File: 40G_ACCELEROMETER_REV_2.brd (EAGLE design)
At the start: 18.8 x 24.1 mm, 30 parts, among them IC1 3.3V_LDO, IC2 X_BUFFER, IC3 Y_BUFFER, IC4 Z_BUFFER

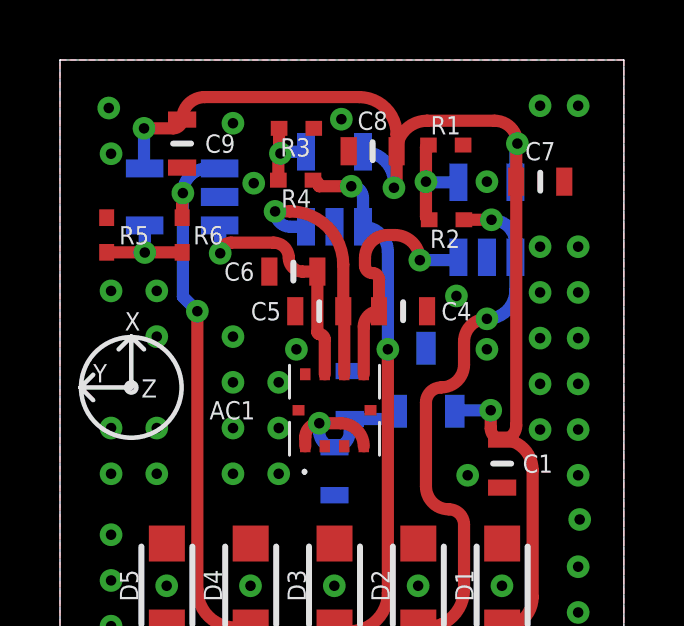
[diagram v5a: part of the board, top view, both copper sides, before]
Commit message: Changes to component label placement. Addition of more ground vias where room was found. Change in routing for power to X buffer
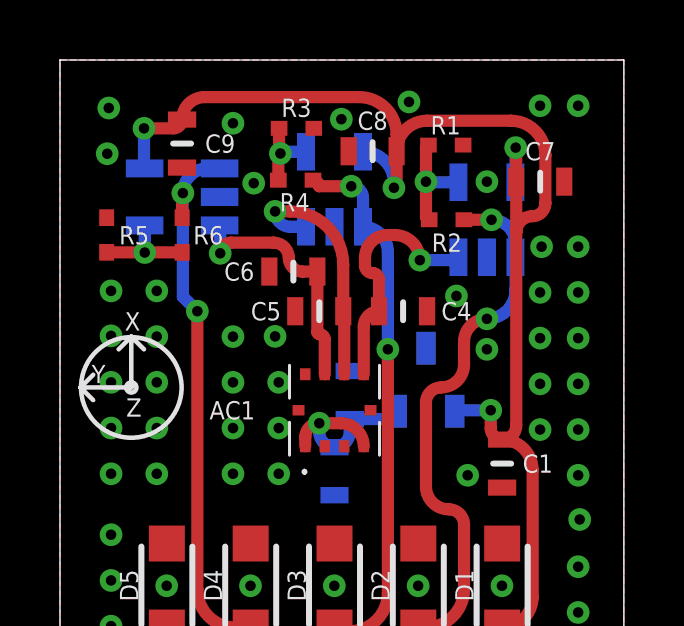
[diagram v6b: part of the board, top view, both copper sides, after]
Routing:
- net 12V: track 42.8 -> 46.4 mm
- net GND: vias 52 -> 56
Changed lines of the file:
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@@
 <wire x1="2.37683125" y1="14.908125" x2="2.800121875" y2="14.484834375" width="0.1524" layer="21"/>
 <wire x1="2.800121875" y1="14.484834375" x2="2.800121875" y2="14.48483125" width="0.1524" layer="21"/>
-<text x="2.7154625" y="12.876328125" size="0.6096" layer="21" font="vector">Z</text>
+<text x="2.2074625" y="12.241328125" size="0.6096" layer="21" font="vector">Z</text>
 <text x="2.159" y="15.113" size="0.6096" layer="21" font="vector">X</text>
-<text x="1.10695625" y="13.384275" size="0.6096" layer="21" font="vector">Y</text>
+<text x="1.05615625" y="13.358875" size="0.6096" layer="21" font="vector">Y</text>
 <text x="14.228975" y="22.019409375" size="0.6096" layer="22" font="vector" rot="MR180" align="center">X-AXIS</text>
 <text x="9.1494875" y="16.685946875" size="0.6096" layer="22" font="vector" rot="MR0" align="center">Y-AXIS</text>
@@
 <attribute name="MANUFACTURER_PART_NUMBER" value="TNPW04023K48BEED" x="12.8842" y="18.804278125" size="1.778" layer="27" rot="R180" display="off"/>
 <attribute name="MFR_NAME" value="Vishay" x="12.8842" y="18.804278125" size="1.778" layer="27" rot="R180" display="off"/>
-<attribute name="NAME" x="12.33388125" y="17.864478125" size="0.6096" layer="25" ratio="6" rot="SR0"/>
+<attribute name="NAME" x="12.89268125" y="18.042278125" size="0.6096" layer="25" ratio="6" rot="SR0" align="center"/>
 </element>
 <element name="R3" library="SamacSys_Parts" package="RES_TNPW0402_VIS" value="TNPW04021K24BEED" x="7.8804" y="21.852278125" smashed="yes">
@@
 <attribute name="MANUFACTURER_PART_NUMBER" value="TNPW04021K24BEED" x="7.8804" y="21.852278125" size="1.778" layer="27" display="off"/>
 <attribute name="MFR_NAME" value="Vishay" x="7.8804" y="21.852278125" size="1.778" layer="27" display="off"/>
-<attribute name="NAME" x="7.347" y="20.912478125" size="0.6096" layer="25" ratio="6" rot="SR0"/>
+<attribute name="NAME" x="7.8804" y="22.538078125" size="0.6096" layer="25" ratio="6" rot="SR0" align="center"/>
 </element>
 <element name="R4" library="SamacSys_Parts" package="RES_TNPW0402_VIS" value="TNPW04023K48BEED" x="7.855" y="20.125078125" smashed="yes" rot="R180">
@@
 <attribute name="MANUFACTURER_PART_NUMBER" value="TNPW04023K48BEED" x="7.855" y="20.125078125" size="1.778" layer="27" rot="R180" display="off"/>
 <attribute name="MFR_NAME" value="Vishay" x="7.855" y="20.125078125" size="1.778" layer="27" rot="R180" display="off"/>
-<attribute name="NAME" x="7.3724" y="19.210678125" size="0.6096" layer="25" ratio="6" rot="SR0"/>
+<attribute name="NAME" x="7.3216" y="19.083678125" size="0.6096" layer="25" ratio="6" rot="SR0"/>
 </element>
 <element name="R5" library="SamacSys_Parts" package="RES_TNPW0402_VIS" value="TNPW04021K24BEED" x="1.5558" y="18.296278125" smashed="yes" rot="R90">
@@
 <via x="14.2304" y="20.074278125" extent="1-16" drill="0.35"/>
 <via x="17.272" y="1.397" extent="1-16" drill="0.35"/>
-<via x="7.8804" y="14.486278125" extent="1-16" drill="0.35"/>
+<via x="7.1692" y="14.918078125" extent="1-16" drill="0.35"/>
 <via x="14.2304" y="14.486278125" extent="1-16" drill="0.35"/>
 <via x="5.7658" y="22.0218" extent="1-16" drill="0.35"/>
 <via x="1.6256" y="22.5298" extent="1-16" drill="0.35"/>
-<via x="1.7018" y="21.0058" extent="1-16" drill="0.35"/>
+<via x="1.5748" y="21.0058" extent="1-16" drill="0.35"/>
 <via x="1.7018" y="16.4338" extent="1-16" drill="0.35"/>
 <via x="3.2258" y="16.4338" extent="1-16" drill="0.35"/>
@@
 <via x="16.002" y="4.191" extent="1-16" drill="0.35"/>
 <via x="16.002" y="11.811" extent="1-16" drill="0.35"/>
-<via x="16.002" y="17.907" extent="1-16" drill="0.35"/>
+<via x="16.0528" y="17.907" extent="1-16" drill="0.35"/>
 <via x="16.002" y="16.383" extent="1-16" drill="0.35"/>
 <via x="16.002" y="14.859" extent="1-16" drill="0.35"/>
@@
 <via x="6.35" y="6.604" extent="1-16" drill="0.35"/>
 <via x="3.556" y="6.604" extent="1-16" drill="0.35"/>
+<via x="3.2258" y="13.3858" extent="1-16" drill="0.35"/>
+<via x="11.6332" y="22.733" extent="1-16" drill="0.35"/>
+<via x="1.7018" y="14.9352" extent="1-16" drill="0.35"/>
+<via x="1.7018" y="13.3858" extent="1-16" drill="0.35"/>
 </signal>
 <signal name="X_SIG">
@@
 <wire x1="8.6424" y1="14.994278125" x2="8.5788" y2="15.057878125" width="0.4064" layer="1" curve="-90"/>
 <wire x1="8.5788" y1="15.057878125" x2="8.5788" y2="17.077078125" width="0.4064" layer="1"/>
-<wire x1="8.5788" y1="17.077078125" x2="8.5788" y2="17.280278125" width="0.4064" layer="1"/>
 <wire x1="8.5788" y1="17.077078125" x2="8.0836" y2="17.077078125" width="0.4064" layer="1"/>
 <wire x1="8.0836" y1="17.077078125" x2="7.6264" y2="17.534278125" width="0.4064" layer="1" curve="-90"/>
@@
 <wire x1="11.2204" y1="21.090278125" x2="11.2204" y2="19.959878125" width="0.4064" layer="1"/>
 <wire x1="11.2204" y1="19.959878125" x2="11.1316" y2="19.871078125" width="0.4064" layer="1" curve="-90"/>
-<wire x1="12.2364" y1="22.106278125" x2="11.2204" y2="21.090278125" width="0.4064" layer="1" curve="90"/>
-<via x="15.2464" y="21.344278125" extent="1-16" drill="0.35"/>
-<wire x1="15.2084" y1="20.074278125" x2="15.2084" y2="21.306278125" width="0.4064" layer="1"/>
-<wire x1="15.2084" y1="21.306278125" x2="15.2464" y2="21.344278125" width="0.4064" layer="1" curve="-90"/>
-<wire x1="15.1804" y1="20.054278125" x2="15.1804" y2="21.278278125" width="0.4064" layer="16"/>
-<wire x1="15.1804" y1="21.278278125" x2="15.2464" y2="21.344278125" width="0.4064" layer="16" curve="-90"/>
-<wire x1="15.2084" y1="20.074278125" x2="15.2084" y2="11.946278125" width="0.4064" layer="1"/>
-<wire x1="15.2084" y1="11.946278125" x2="14.7384" y2="11.476278125" width="0.4064" layer="1" curve="-90"/>
+<wire x1="14.7384" y1="11.476278125" x2="15.2084" y2="11.946278125" width="0.4064" layer="1" curve="90"/>
 <wire x1="14.7384" y1="2.294278125" x2="14.7384" y2="5.212278125" width="0.4064" layer="1"/>
 <wire x1="14.7384" y1="5.212278125" x2="15.7544" y2="6.228278125" width="0.4064" layer="1" curve="90"/>
 <wire x1="15.7544" y1="10.460278125" x2="14.7384" y2="11.476278125" width="0.4064" layer="1" curve="90"/>
 <wire x1="15.7544" y1="6.228278125" x2="15.7544" y2="10.460278125" width="0.4064" layer="1"/>
-<wire x1="15.2464" y1="21.344278125" x2="14.4844" y2="22.106278125" width="0.4064" layer="1" curve="90"/>
-<wire x1="14.4844" y1="22.106278125" x2="12.2364" y2="22.106278125" width="0.4064" layer="1"/>
-<wire x1="11.2204" y1="21.090278125" x2="11.2204" y2="21.242678125" width="0.4064" layer="1"/>
 <via x="2.8004" y="21.852278125" extent="1-16" drill="0.35"/>
 <wire x1="4.0704" y1="22.144278125" x2="3.7784" y2="21.852278125" width="0.4064" layer="1" curve="-90"/>
@@
 <wire x1="13.1584" y1="12.420278125" x2="13.1924" y2="12.454278125" width="0.4064" layer="16" curve="-90"/>
 <wire x1="13.1924" y1="12.454278125" x2="14.3574" y2="12.454278125" width="0.4064" layer="16"/>
-<wire x1="11.2204" y1="21.090278125" x2="11.2204" y2="21.649078125" width="0.4064" layer="1"/>
 <wire x1="11.2204" y1="21.649078125" x2="9.9758" y2="22.893678125" width="0.4064" layer="1" curve="90"/>
 <wire x1="4.8198" y1="22.893678125" x2="4.0704" y2="22.144278125" width="0.4064" layer="1" curve="90"/>
 <wire x1="9.9758" y1="22.893678125" x2="4.8198" y2="22.893678125" width="0.4064" layer="1"/>
+<wire x1="15.2084" y1="11.946278125" x2="15.2084" y2="18.3834" width="0.4064" layer="1"/>
+<wire x1="15.748" y1="18.923" x2="15.2084" y2="18.3834" width="0.4064" layer="1" curve="90"/>
+<wire x1="15.748" y1="18.923" x2="16.1798" y2="19.3548" width="0.4064" layer="1" curve="90"/>
+<wire x1="16.1798" y1="19.3548" x2="16.1798" y2="20.955" width="0.4064" layer="1"/>
+<wire x1="16.1798" y1="20.955" x2="15.028521875" y2="22.106278125" width="0.4064" layer="1" curve="90"/>
+<wire x1="15.028521875" y1="22.106278125" x2="12.2364" y2="22.106278125" width="0.4064" layer="1"/>
+<via x="15.1892" y="21.209" extent="1-16" drill="0.35"/>
+<wire x1="15.2084" y1="18.3834" x2="15.2084" y2="20.074278125" width="0.4064" layer="1"/>
+<wire x1="15.2084" y1="20.074278125" x2="15.2084" y2="21.1898" width="0.4064" layer="1"/>
+<wire x1="15.2084" y1="21.1898" x2="15.1892" y2="21.209" width="0.4064" layer="1" curve="90"/>
+<wire x1="15.1804" y1="20.054278125" x2="15.1804" y2="21.2002" width="0.4064" layer="16"/>
+<wire x1="15.1804" y1="21.2002" x2="15.1892" y2="21.209" width="0.4064" layer="16" curve="90"/>
+<wire x1="11.2204" y1="21.090278125" x2="11.2204" y2="21.649078125" width="0.4064" layer="1"/>
+<wire x1="11.2204" y1="21.090278125" x2="12.2364" y2="22.106278125" width="0.4064" layer="1" curve="-90"/>
 </signal>
 <signal name="X_OUT">

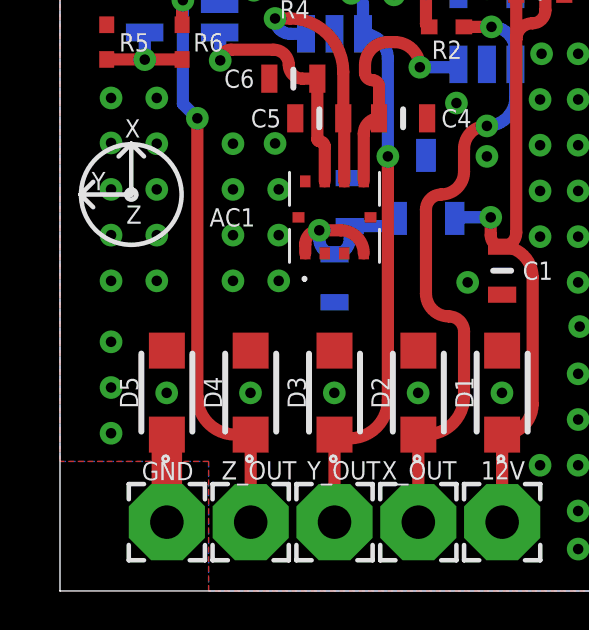
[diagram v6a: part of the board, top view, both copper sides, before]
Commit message: Widened GND path near diode. Enlarged Z dot for board orientation.
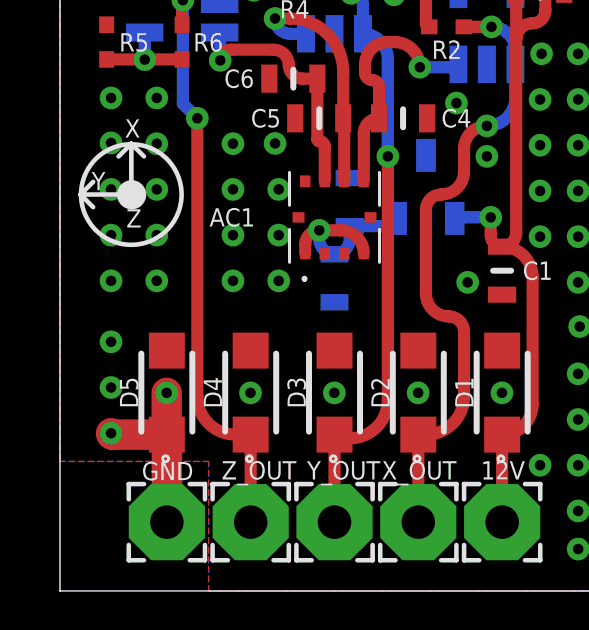
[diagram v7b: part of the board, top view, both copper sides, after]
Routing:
- net GND: track 2.92 -> 6.19 mm
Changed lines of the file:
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@@
 <drawing>
 <settings>
-<setting alwaysvectorfont="yes"/>
+<setting alwaysvectorfont="no"/>
 <setting verticaltext="up"/>
 </settings>
@@
 <wire x1="2.37683125" y1="14.908125" x2="2.800121875" y2="14.484834375" width="0.1524" layer="21"/>
 <wire x1="2.800121875" y1="14.484834375" x2="2.800121875" y2="14.48483125" width="0.1524" layer="21"/>
-<text x="2.2074625" y="12.241328125" size="0.6096" layer="21" font="vector">Z</text>
+<text x="2.2074625" y="12.114328125" size="0.6096" layer="21" font="vector">Z</text>
 <text x="2.159" y="15.113" size="0.6096" layer="21" font="vector">X</text>
 <text x="1.05615625" y="13.358875" size="0.6096" layer="21" font="vector">Y</text>
@@
 <text x="9.1494875" y="16.685946875" size="0.6096" layer="22" font="vector" rot="MR0" align="center">Y-AXIS</text>
 <text x="4.06999375" y="16.6012875" size="0.6096" layer="22" font="vector" rot="MR180" align="center">Z-AXIS</text>
+<circle x="2.3876" y="13.208" radius="0.0254" width="0.1524" layer="21"/>
+<circle x="2.3876" y="13.208" radius="0.26518125" width="0.1524" layer="21"/>
+<circle x="2.3876" y="13.208" radius="0.410346875" width="0.1524" layer="21"/>
 </plain>
 <attributes>
@@
 <via x="1.7018" y="14.9352" extent="1-16" drill="0.35"/>
 <via x="1.7018" y="13.3858" extent="1-16" drill="0.35"/>
+<wire x1="3.5624" y1="5.212278125" x2="3.556" y2="5.218678125" width="1.016" layer="1" curve="-90"/>
+<wire x1="3.556" y1="5.218678125" x2="3.556" y2="6.604" width="1.016" layer="1"/>
+<wire x1="3.5624" y1="5.212278125" x2="1.747321875" y2="5.212278125" width="1.016" layer="1"/>
+<wire x1="1.747321875" y1="5.212278125" x2="1.7018" y2="5.2578" width="1.016" layer="1" curve="-90"/>
 </signal>
 <signal name="X_SIG">
